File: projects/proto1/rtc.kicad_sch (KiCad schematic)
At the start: 2 parts, among them U28 MC146818P

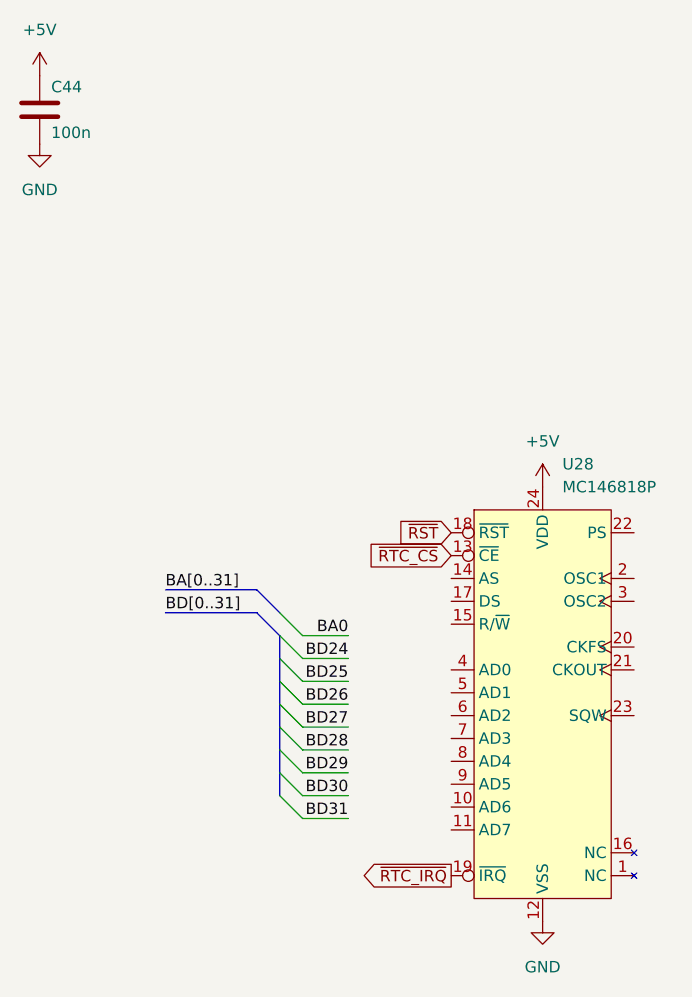
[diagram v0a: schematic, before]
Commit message: Renamed CMC to SCU, changed verification method to cocotb, and modified pcb schematic
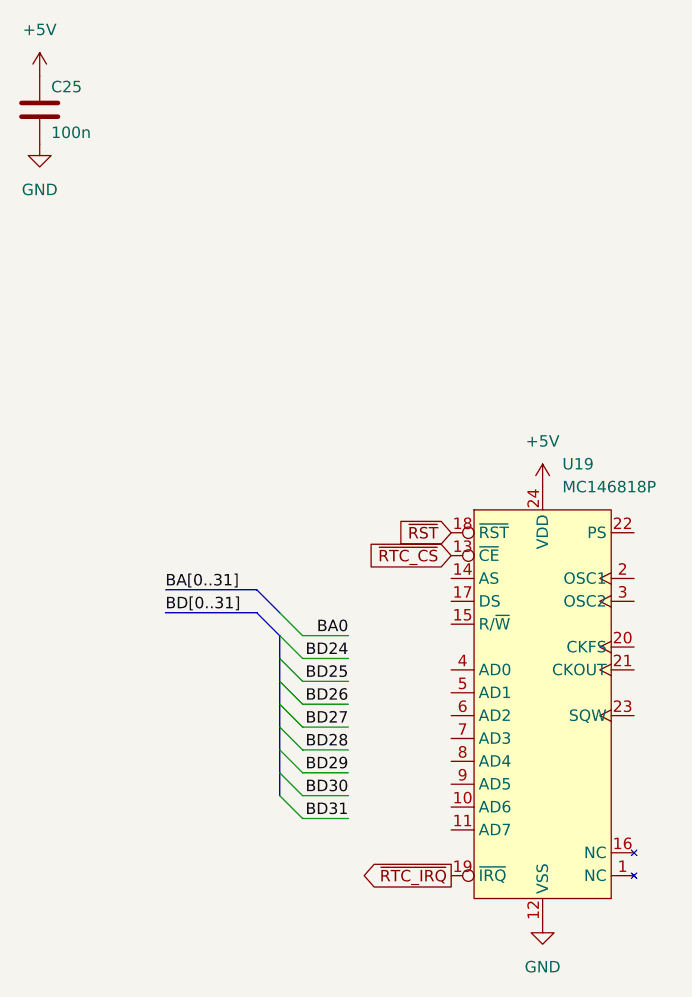
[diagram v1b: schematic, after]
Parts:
- renumbered C44 to C25, U28 to U19
